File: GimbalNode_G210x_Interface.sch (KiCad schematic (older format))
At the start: 4 parts

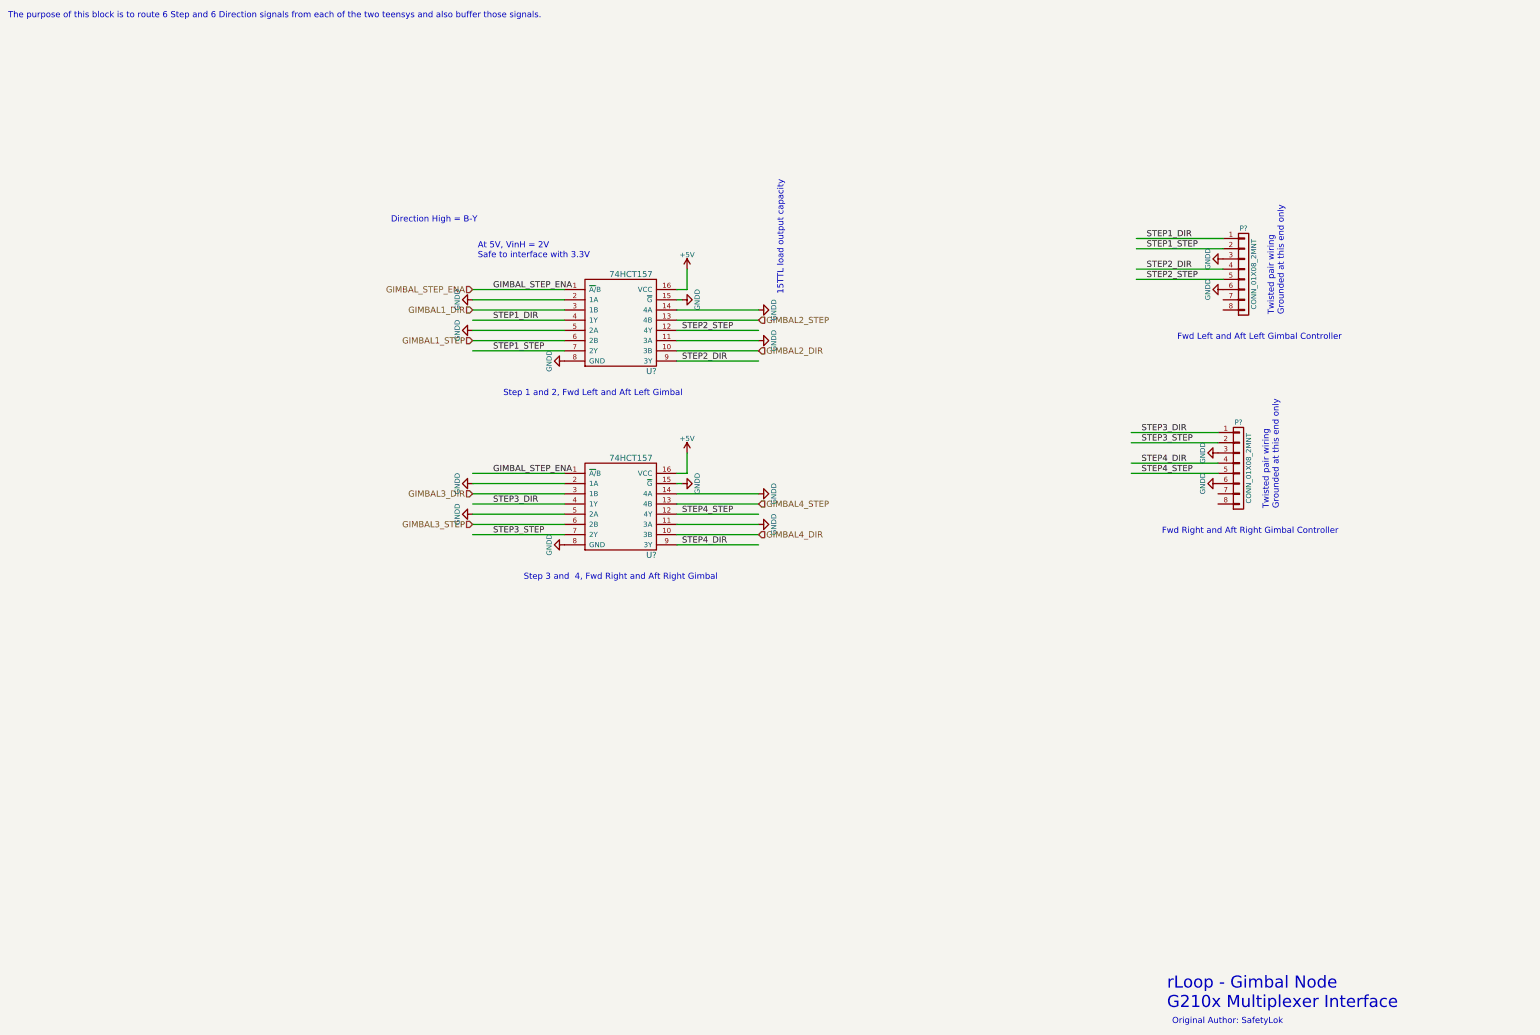
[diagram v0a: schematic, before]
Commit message: Fixup various caps on 4-20ma sheet.
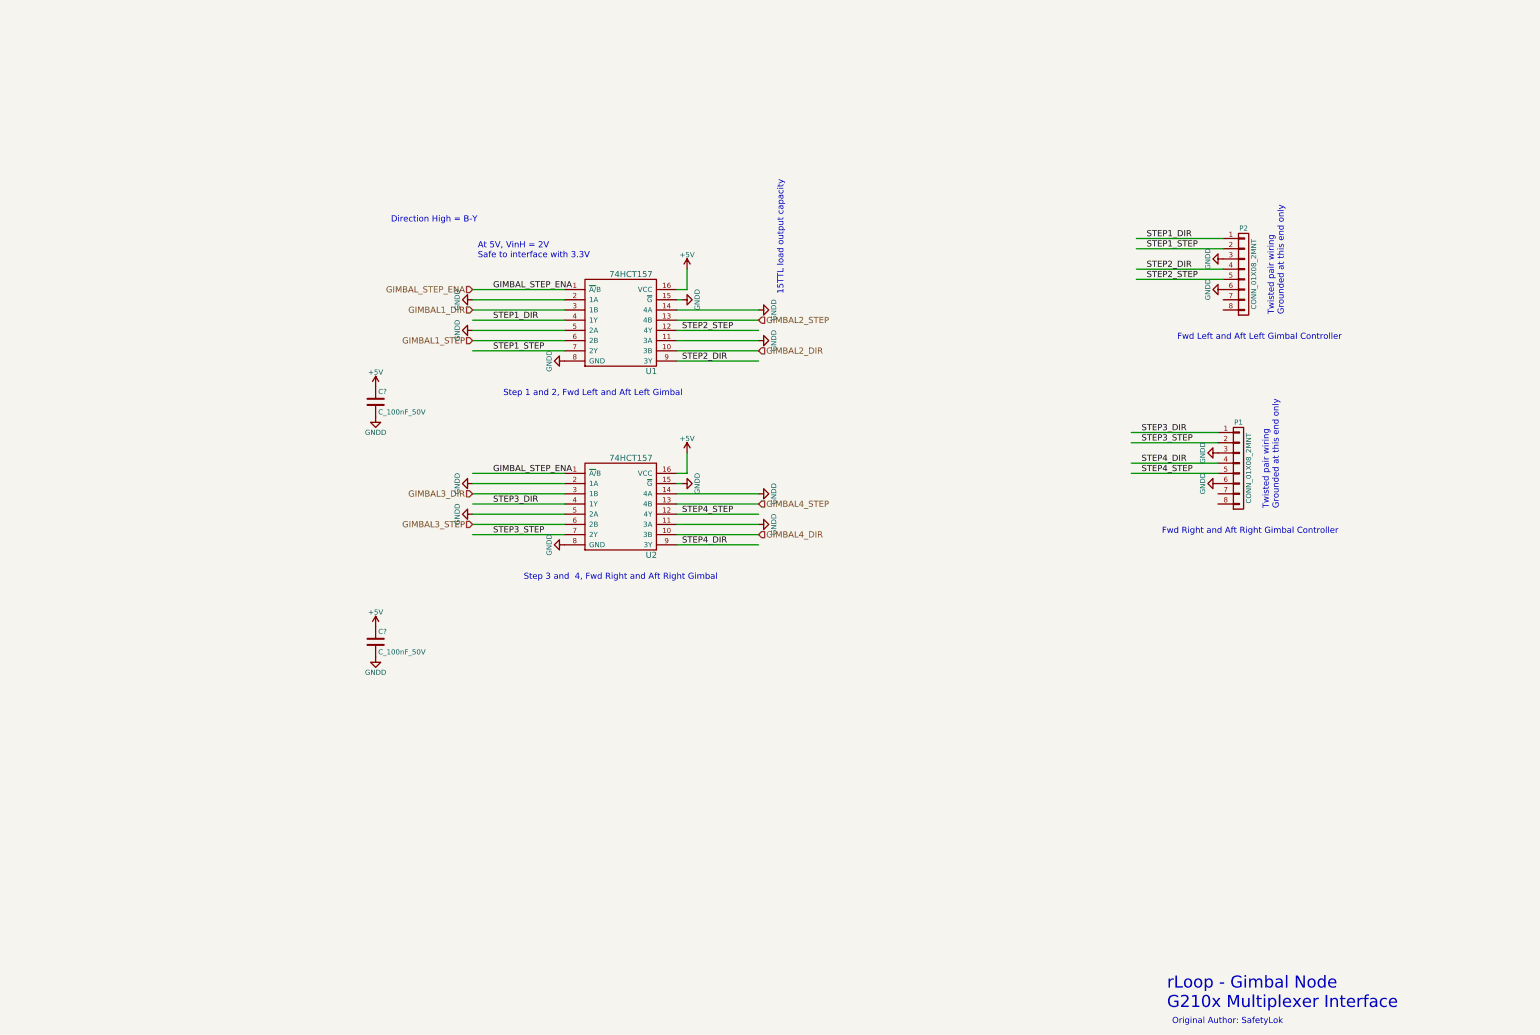
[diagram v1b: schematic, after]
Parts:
- added C? (x2): C_100nF_50V, RLOOP_FOOTPRINTS:rLoop_C_0603, symbol C_100nF_50V
- gave numbers to parts that had none: 4
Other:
- note removed: "The purpose of this block is to route 6 Step and 6 Direction signals from each of the two teensys and also buffer those signals.\n"
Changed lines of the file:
@@
 rLoop - Gimbal Node\nG210x Multiplexer Interface
 $Comp
-L CONN_01X08_2MNT P?
+L CONN_01X08_2MNT P2
 U 1 1 5757EB8A
 P 12700 3150
-F 0 "P?" H 12700 3600 50  0000 C CNN
+F 0 "P2" H 12700 3600 50  0000 C CNN
 F 1 "CONN_01X08_2MNT" V 12800 3150 50  0000 C CNN
 F 2 "" H 12700 3150 50  0000 C CNN
@@
 	1    0    0    -1
 $EndComp
-Text Notes 600  650  0    60   ~ 0
-The purpose of this block is to route 6 Step and 6 Direction signals from each of the two teensys and also buffer those signals.\n
 Text Notes 5450 4350 0    60   ~ 0
 Step 1 and 2, Fwd Left and Aft Left Gimbal
@@
 	12500 3200 11650 3200
 $Comp
-L GNDD #PWR?
+L GNDD #PWR05
 U 1 1 5757EB8B
 P 12500 3000
-F 0 "#PWR?" H 12500 2750 50  0001 C CNN
+F 0 "#PWR05" H 12500 2750 50  0001 C CNN
 F 1 "GNDD" H 12500 2850 50  0000 C CNN
 F 2 "" H 12500 3000 50  0000 C CNN
@@
 $EndComp
 $Comp
-L GNDD #PWR?
+L GNDD #PWR06
 U 1 1 5757EB8C
 P 12500 3300
-F 0 "#PWR?" H 12500 3050 50  0001 C CNN
+F 0 "#PWR06" H 12500 3050 50  0001 C CNN
 F 1 "GNDD" H 12500 3150 50  0000 C CNN
 F 2 "" H 12500 3300 50  0000 C CNN
@@
 Twisted pair wiring\nGrounded at this end only
 $Comp
-L CONN_01X08_2MNT P?
+L CONN_01X08_2MNT P1
 U 1 1 5757EB8D
 P 12650 5050
-F 0 "P?" H 12650 5500 50  0000 C CNN
+F 0 "P1" H 12650 5500 50  0000 C CNN
 F 1 "CONN_01X08_2MNT" V 12750 5050 50  0000 C CNN
 F 2 "" H 12650 5050 50  0000 C CNN
@@
 	12450 5100 11600 5100
 $Comp
-L GNDD #PWR?
+L GNDD #PWR07
 U 1 1 5757EB8E
 P 12450 4900
-F 0 "#PWR?" H 12450 4650 50  0001 C CNN
+F 0 "#PWR07" H 12450 4650 50  0001 C CNN
 F 1 "GNDD" H 12450 4750 50  0000 C CNN
 F 2 "" H 12450 4900 50  0000 C CNN
@@
 $EndComp
 $Comp
-L GNDD #PWR?
+L GNDD #PWR08
 U 1 1 5757EB8F
 P 12450 5200
-F 0 "#PWR?" H 12450 4950 50  0001 C CNN
+F 0 "#PWR08" H 12450 4950 50  0001 C CNN
 F 1 "GNDD" H 12450 5050 50  0000 C CNN
 F 2 "" H 12450 5200 50  0000 C CNN
@@
 Original Author: SafetyLok
 $Comp
-L 74HCT157 U?
+L 74HCT157 U1
 U 1 1 5757EB93
 P 6250 4050
-F 0 "U?" H 6900 4000 59  0000 C CNN
+F 0 "U1" H 6900 4000 59  0000 C CNN
 F 1 "74HCT157" H 6700 4950 59  0000 C CNN
 F 2 "" H 6250 4050 197 0000 C CNN
@@
 	6050 3900 5150 3900
 $Comp
-L GNDD #PWR?
+L GNDD #PWR09
 U 1 1 5757EB94
 P 7200 3400
-F 0 "#PWR?" H 7200 3150 50  0001 C CNN
+F 0 "#PWR09" H 7200 3150 50  0001 C CNN
 F 1 "GNDD" H 7200 3250 50  0000 C CNN
 F 2 "" H 7200 3400 50  0000 C CNN
@@
 	7150 3400 7200 3400
 $Comp
-L GNDD #PWR?
+L GNDD #PWR010
 U 1 1 5757EB95
 P 6050 4000
-F 0 "#PWR?" H 6050 3750 50  0001 C CNN
+F 0 "#PWR010" H 6050 3750 50  0001 C CNN
 F 1 "GNDD" H 6050 3850 50  0000 C CNN
 F 2 "" H 6050 4000 50  0000 C CNN
@@
 GIMBAL_STEP_ENA
 $Comp
-L +5V #PWR?
+L +5V #PWR011
 U 1 1 5757EB96
 P 7250 3100
-F 0 "#PWR?" H 7250 2950 50  0001 C CNN
+F 0 "#PWR011" H 7250 2950 50  0001 C CNN
 F 1 "+5V" H 7250 3240 50  0000 C CNN
 F 2 "" H 7250 3100 50  0000 C CNN
@@
 $EndComp
 $Comp
-L 74HCT157 U?
+L 74HCT157 U2
 U 1 1 5757EB97
 P 6250 5850
-F 0 "U?" H 6900 5800 59  0000 C CNN
+F 0 "U2" H 6900 5800 59  0000 C CNN
 F 1 "74HCT157" H 6700 6750 59  0000 C CNN
 F 2 "" H 6250 5850 197 0000 C CNN
@@
 	6050 5700 5150 5700
 $Comp
-L GNDD #PWR?
+L GNDD #PWR012
 U 1 1 5757EB98
 P 7200 5200
-F 0 "#PWR?" H 7200 4950 50  0001 C CNN
+F 0 "#PWR012" H 7200 4950 50  0001 C CNN
 F 1 "GNDD" H 7200 5050 50  0000 C CNN
 F 2 "" H 7200 5200 50  0000 C CNN
@@
 Wire Wire Line
 	7150 5200 7200 5200
-$Comp
-L GNDD #PWR?
-U 1 1 5757EB99
-P 6050 5800
-F 0 "#PWR?" H 6050 5550 50  0001 C CNN
-F 1 "GNDD" H 6050 5650 50  0000 C CNN
-F 2 "" H 6050 5800 50  0000 C CNN
-F 3 "" H 6050 5800 50  0000 C CNN
-	1    6050 5800
-	0    1    1    0
-$EndComp
 Text Label 7200 5800 0    60   ~ 0
 STEP4_DIR
@@
 GIMBAL_STEP_ENA
 $Comp
-L +5V #PWR?
+L +5V #PWR013
 U 1 1 5757EB9A
 P 7250 4900
-F 0 "#PWR?" H 7250 4750 50  0001 C CNN
+F 0 "#PWR013" H 7250 4750 50  0001 C CNN
 F 1 "+5V" H 7250 5040 50  0000 C CNN
 F 2 "" H 7250 4900 50  0000 C CNN
@@
 STEP4_STEP
 $Comp
-L GNDD #PWR?
+L GNDD #PWR014
 U 1 1 5757F02C
 P 5150 3400
-F 0 "#PWR?" H 5150 3150 50  0001 C CNN
+F 0 "#PWR014" H 5150 3150 50  0001 C CNN
 F 1 "GNDD" H 5150 3250 50  0000 C CNN
 F 2 "" H 5150 3400 50  0000 C CNN
@@
 $EndComp
 $Comp
-L GNDD #PWR?
+L GNDD #PWR015
 U 1 1 5757F037
 P 5150 3700
-F 0 "#PWR?" H 5150 3450 50  0001 C CNN
+F 0 "#PWR015" H 5150 3450 50  0001 C CNN
 F 1 "GNDD" H 5150 3550 50  0000 C CNN
 F 2 "" H 5150 3700 50  0000 C CNN
@@
 $EndComp
 $Comp
-L GNDD #PWR?
+L GNDD #PWR016
 U 1 1 5757F042
 P 5150 5200
-F 0 "#PWR?" H 5150 4950 50  0001 C CNN
+F 0 "#PWR016" H 5150 4950 50  0001 C CNN
 F 1 "GNDD" H 5150 5050 50  0000 C CNN
 F 2 "" H 5150 5200 50  0000 C CNN
@@
 $EndComp
 $Comp
-L GNDD #PWR?
+L GNDD #PWR017
 U 1 1 5757F04D
 P 5150 5500
-F 0 "#PWR?" H 5150 5250 50  0001 C CNN
+F 0 "#PWR017" H 5150 5250 50  0001 C CNN
 F 1 "GNDD" H 5150 5350 50  0000 C CNN
 F 2 "" H 5150 5500 50  0000 C CNN
@@
 $EndComp
 $Comp
-L GNDD #PWR?
+L GNDD #PWR018
 U 1 1 5757F058
 P 7950 3500
-F 0 "#PWR?" H 7950 3250 50  0001 C CNN
+F 0 "#PWR018" H 7950 3250 50  0001 C CNN
 F 1 "GNDD" H 7950 3350 50  0000 C CNN
 F 2 "" H 7950 3500 50  0000 C CNN
@@
 $EndComp
 $Comp
-L GNDD #PWR?
+L GNDD #PWR019
 U 1 1 5757F063
 P 7950 3800
-F 0 "#PWR?" H 7950 3550 50  0001 C CNN
+F 0 "#PWR019" H 7950 3550 50  0001 C CNN
 F 1 "GNDD" H 7950 3650 50  0000 C CNN
 F 2 "" H 7950 3800 50  0000 C CNN
@@
 $EndComp
 $Comp
-L GNDD #PWR?
+L GNDD #PWR020
 U 1 1 5757F078
 P 7950 5300
-F 0 "#PWR?" H 7950 5050 50  0001 C CNN
+F 0 "#PWR020" H 7950 5050 50  0001 C CNN
 F 1 "GNDD" H 7950 5150 50  0000 C CNN
 F 2 "" H 7950 5300 50  0000 C CNN
@@
 $EndComp
 $Comp
-L GNDD #PWR?
+L GNDD #PWR021
 U 1 1 5757F083
 P 7950 5600
-F 0 "#PWR?" H 7950 5350 50  0001 C CNN
+F 0 "#PWR021" H 7950 5350 50  0001 C CNN
 F 1 "GNDD" H 7950 5450 50  0000 C CNN
 F 2 "" H 7950 5600 50  0000 C CNN
@@
 	0    -1   -1   0
 $EndComp
+$Comp
+L GNDD #PWR022
+U 1 1 5758A913
+P 6050 5800
+F 0 "#PWR022" H 6050 5550 50  0001 C CNN
+F 1 "GNDD" H 6050 5650 50  0000 C CNN
+F 2 "" H 6050 5800 50  0000 C CNN
+F 3 "" H 6050 5800 50  0000 C CNN
+	1    6050 5800
+	0    1    1    0
+$EndComp
+$Comp
+L GNDD #PWR023
+U 1 1 5758AA2C
+P 4200 4550
+F 0 "#PWR023" H 4200 4300 50  0001 C CNN
+F 1 "GNDD" H 4200 4400 50  0000 C CNN
+F 2 "" H 4200 4550 50  0000 C CNN
+F 3 "" H 4200 4550 50  0000 C CNN
+	1    4200 4550
+	1    0    0    -1
+$EndComp
+$Comp
+L +5V #PWR024
+U 1 1 5758AA38
+P 4200 4250
+F 0 "#PWR024" H 4200 4100 50  0001 C CNN
+F 1 "+5V" H 4200 4390 50  0000 C CNN
+F 2 "" H 4200 4250 50  0000 C CNN
+F 3 "" H 4200 4250 50  0000 C CNN
+	1    4200 4250
+	1    0    0    -1
+$EndComp
+$Comp
+L GNDD #PWR025
+U 1 1 5758AAB6
+P 4200 6900
+F 0 "#PWR025" H 4200 6650 50  0001 C CNN
+F 1 "GNDD" H 4200 6750 50  0000 C CNN
+F 2 "" H 4200 6900 50  0000 C CNN
+F 3 "" H 4200 6900 50  0000 C CNN
+	1    4200 6900
+	1    0    0    -1
+$EndComp
+$Comp
+L +5V #PWR026
+U 1 1 5758AAC2
+P 4200 6600
+F 0 "#PWR026" H 4200 6450 50  0001 C CNN
+F 1 "+5V" H 4200 6740 50  0000 C CNN
+F 2 "" H 4200 6600 50  0000 C CNN
+F 3 "" H 4200 6600 50  0000 C CNN
+	1    4200 6600
+	1    0    0    -1
+$EndComp
+$Comp
+L C_100nF_50V C?
+U 1 1 5758DE9D
+P 4200 4400
+F 0 "C?" H 4225 4500 50  0000 L CNN
+F 1 "C_100nF_50V" H 4225 4300 50  0000 L CNN
+F 2 "RLOOP_FOOTPRINTS:rLoop_C_0603" H 4238 4250 50  0001 C CNN
+F 3 "" H 4200 4400 50  0000 C CNN
+	1    4200 4400
+	1    0    0    -1
+$EndComp
+$Comp
+L C_100nF_50V C?
+U 1 1 5758DF8E
+P 4200 6750
+F 0 "C?" H 4225 6850 50  0000 L CNN
+F 1 "C_100nF_50V" H 4225 6650 50  0000 L CNN
+F 2 "RLOOP_FOOTPRINTS:rLoop_C_0603" H 4238 6600 50  0001 C CNN
+F 3 "" H 4200 6750 50  0000 C CNN
+	1    4200 6750
+	1    0    0    -1
+$EndComp
 $EndSCHEMATC
